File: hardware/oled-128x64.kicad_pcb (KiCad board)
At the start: 2 copper layers, 40 x 40 mm, 34 parts, among them P1 CON-SENSOR2, P2 DEBUG, P3 BOOT, U1 XMC130024, U3 OLED013, U4 DRILL, U5 DRILL, U6 DRILL, U7 DRILL

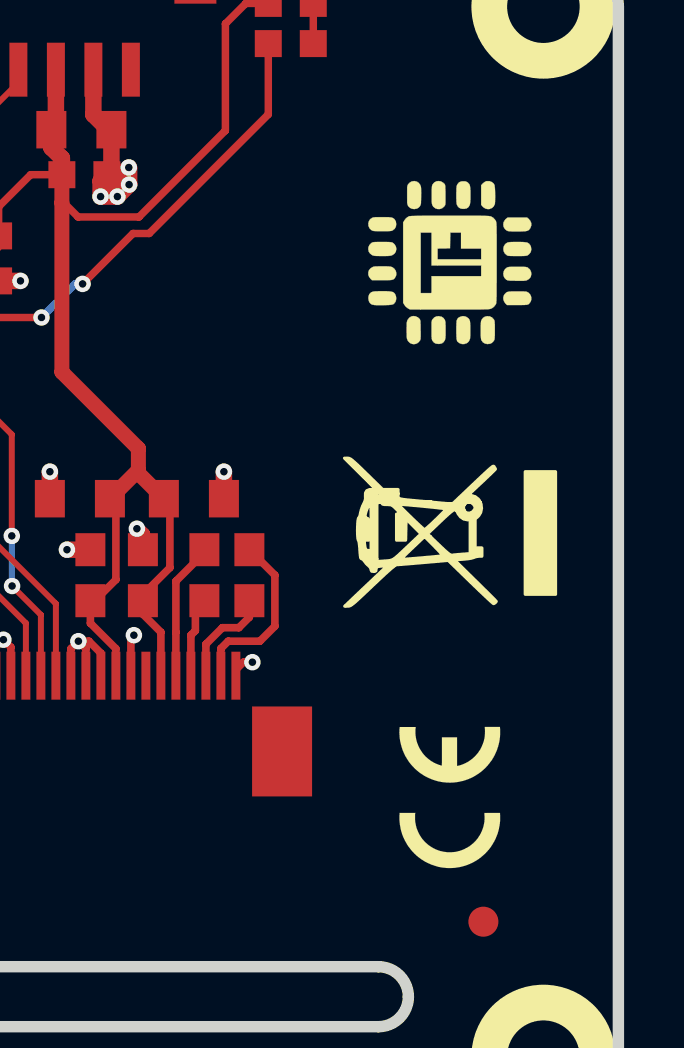
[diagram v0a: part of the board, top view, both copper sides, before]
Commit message: Fix orientation of our logos
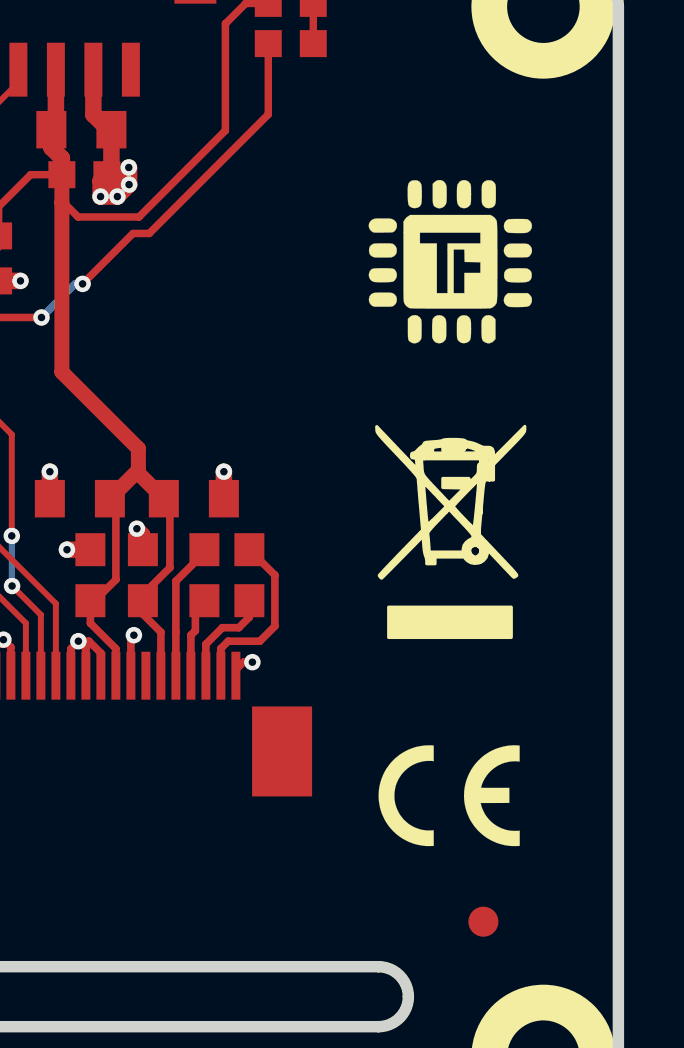
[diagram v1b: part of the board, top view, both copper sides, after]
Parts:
- turned G*** to 0 degrees (x2)
- turned VAL to 0 degrees
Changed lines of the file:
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@@
     (links 78)
     (no_connects 0)
-    (area 133.244999 120.744999 174.955001 162.455001)
+    (area 133.909499 121.409499 174.290501 161.790501)
     (thickness 1.6)
     (drawings 24)
@@
   )
   (module kicad-libraries:CE_5mm (layer F.Cu)
-    (at 168.48 150.42 90)
-    (fp_text reference VAL (at 0 0 90) (layer F.SilkS) hide
+    (at 168.5 150.4)
+    (fp_text reference VAL (at 0 0) (layer F.SilkS) hide
       (effects (font (size 0.2 0.2) (thickness 0.05)))
     )
-    (fp_text value CE_5mm (at 0 0 90) (layer F.SilkS) hide
+    (fp_text value CE_5mm (at 0 0) (layer F.SilkS) hide
       (effects (font (size 0.2 0.2) (thickness 0.05)))
     )
@@
   )
   (module kicad-libraries:WEEE_7mm (layer F.Cu)
-    (at 168.48 141.63 90)
-    (fp_text reference G*** (at 0 0 90) (layer F.SilkS) hide
+    (at 168.5 141.6)
+    (fp_text reference G*** (at 0 0) (layer F.SilkS) hide
       (effects (font (size 0.2 0.2) (thickness 0.05)))
     )
-    (fp_text value LOGO (at 0.75 0 90) (layer F.SilkS) hide
+    (fp_text value LOGO (at 0.75 0) (layer F.SilkS) hide
       (effects (font (size 0.2 0.2) (thickness 0.05)))
     )
@@
   )
   (module kicad-libraries:Logo_CoMCU (layer F.Cu)
-    (at 168.48 132.63 90)
-    (fp_text reference G*** (at 0 0 90) (layer F.SilkS) hide
+    (at 168.5 132.6)
+    (fp_text reference G*** (at 0 0) (layer F.SilkS) hide
       (effects (font (thickness 0.3)))
     )
-    (fp_text value LOGO (at 0.75 0 90) (layer F.SilkS) hide
+    (fp_text value LOGO (at 0.75 0) (layer F.SilkS) hide
       (effects (font (thickness 0.3)))
     )
